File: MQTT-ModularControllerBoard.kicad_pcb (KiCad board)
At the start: 4 copper layers, 200 x 45 mm, 86 parts, among them IC301 LM74700QDBVTQ1, IC401 TPS563200DDCR, IC402 LM74700QDBVTQ1, J301 1715721, J501 A2541HWV-10P, J502 A2541HWV-10P, J503 A2541HWV-10P, J504 A2541HWV-10P, J505 A2541HWV-10P, J506 A2541HWV-10P, J507 A2541HWV-10P, J508 A2541HWV-10P, J601 1051640001, Q301 60V 38A, Q401 60V 38A, U201 ESP32-S3-WROOM-1U-N16R8, U401 LDO 3.3V 1A, U601 ESD Protection IC

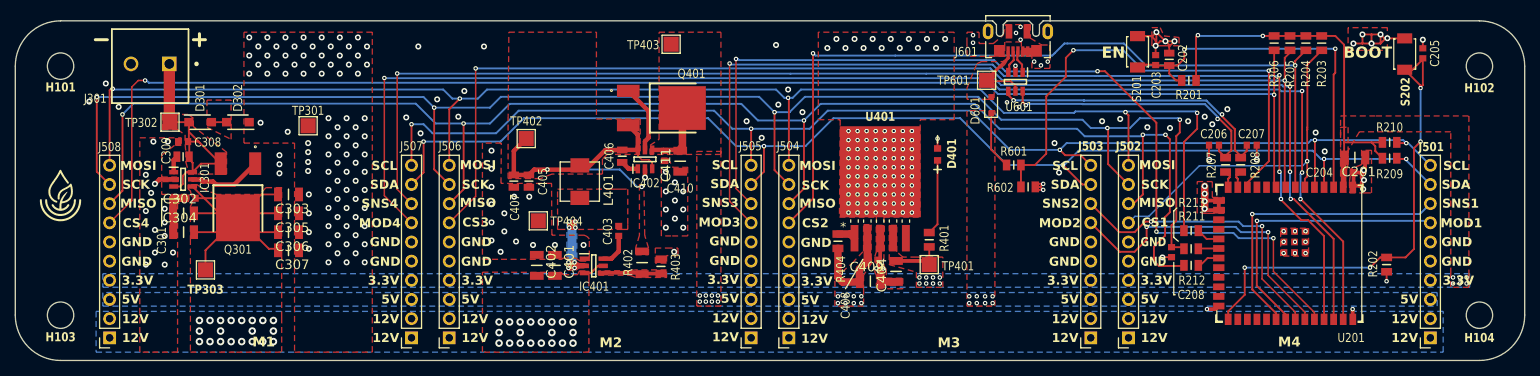
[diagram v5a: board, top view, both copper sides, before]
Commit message: Swapped MCP1826 with a TLV767, and updated the layout and silkscreen to match it.
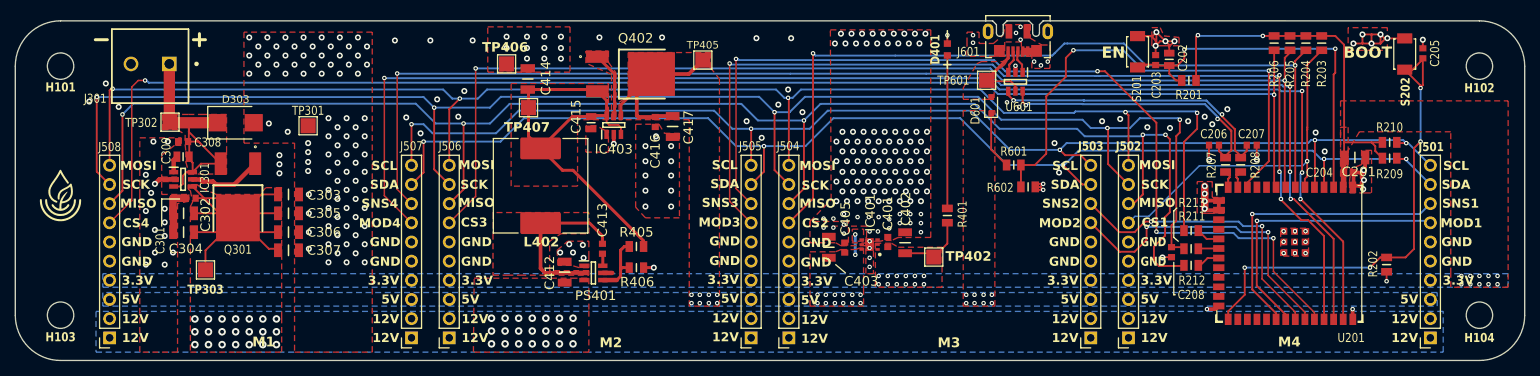
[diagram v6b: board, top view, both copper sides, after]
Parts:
- removed C404, C409, C411: 10uF 10% 25V, JLCPCB Basic:CAPC3216X180N
- removed C406: 220nF 10% 50V, JLCPCB Basic:CAPC2012X135N
- removed C407: 22uF 20% 25V, JLCPCB Basic:CAPC2012X75N
- removed C408, C410: 0.1uF 10% 50V, JLCPCB Basic:CAPC1608X90N
- removed D301, D302: 13.3V 0.1uA Leak, LITTELFUSE Diodes:SODFL3619X98N
- removed IC402: LM74700QDBVTQ1, TEXAS INSTRUMENTS ICs:SOT95P280X145-6N
- removed L401: 3.3uH 6.3A 20%, KOHERELEC Inductors:SMD57x52mm
- removed Q401: 60V 38A, ONSEMI Transistors:DPAK__SINGLE-GAUGE__TO-252_369C__ISSUE_F
- removed R402: 56kΩ 1/4W 1%, YAGEO Resistors:RESC3116X65N
- removed R403, R404: 10kΩ 1/8W 1%, JLCPCB Basic:RESC2013X65N
- removed TP401, TP403, TP404: TestPoint, TestPoint:TestPoint_Pad_2.0x2.0mm
- removed U401: LDO 3.3V 1A, MICROCHIPTECH Low Dropout Regulators:DDPAK5_MC_MCH
- added C412: 10uF 10% 25V, JLCPCB Basic:CAPC3216X180N, F.Cu at (120.3, 124.8)
- added C413: 0.1uF 10% 50V, JLCPCB Basic:CAPC1608X90N, F.Cu at (125.3, 121.7)
- added C414: 47uF 20% 10V, JLCPCB Basic:CAPC3216X190N, F.Cu at (115.4, 99.2)
- added C415: 220nF 10% 50V, JLCPCB Basic:CAPC2012X135N, F.Cu at (123.8, 105.0)
- added C416: 0.1uF 10% 50V, JLCPCB Basic:CAPC1608X90N, F.Cu at (132.3, 104.9)
- added C417: 10uF 10% 25V, JLCPCB Basic:CAPC3216X180N, F.Cu at (134.6, 105.5)
- added D303: 13V 21.5V 1uA Leak, LITTELFUSE Diodes:DO-214AA_Bidirectional, F.Cu at (76.7, 105.0)
- added IC403: LM74700QDBVTQ1, TEXAS INSTRUMENTS ICs:SOT95P280X145-6N, F.Cu at (126.8, 105.3)
- added L402: 10uH, 5.4A, 20%, Inductor_SMD:L_SXN_SMDRI127, F.Cu at (117.1, 113.3)
- added PS401: TPS54308DDCR, TEXAS INSTRUMENTS ICs:SOT95P280X110-6N, F.Cu at (124.1, 124.9)
- added Q402: 60V 38A, ONSEMI Transistors:DPAK__SINGLE-GAUGE__TO-252_369C__ISSUE_F, F.Cu at (133.6, 98.5)
- added R405: 100kΩ 1/8W 1%, JLCPCB Basic:RESC2013X65N, F.Cu at (129.8, 121.4)
- added R406: 13.7kΩ 1/8W 1%, YAGEO Resistors:RESC2012X60N, F.Cu at (129.8, 124.2)
- added TP405: TestPoint, TestPoint:TestPoint_Pad_2.0x2.0mm, F.Cu at (138.6, 96.7)
- added TP406: TestPoint, TestPoint:TestPoint_Pad_2.0x2.0mm, F.Cu at (112.6, 97.2)
- added TP407: TestPoint, TestPoint:TestPoint_Pad_2.0x2.0mm, F.Cu at (115.5, 103.0)
- C401: value 10uF 10% 25V -> 0.1uF 10% 50V; footprint JLCPCB Basic:CAPC3216X180N -> JLCPCB Basic:CAPC1608X90N
- C405: value 22uF 20% 25V -> 10uF 10% 25V; footprint JLCPCB Basic:CAPC2012X75N -> JLCPCB Basic:CAPC3216X180N
- IC401: value TPS563200DDCR -> TLV76733DRVR; footprint TEXAS INSTRUMENTS ICs:SOT95P280X110-6N -> TEXAS INSTRUMENTS ICs:SON65P200X200X80-7N
- moved TP402 56.2 mm to (169.2, 122.8), turned to 0 degrees
- moved C402 48.9 mm to (165.4, 120.9)
- moved C401 44.2 mm to (163.1, 120.8), turned to 90 degrees
- moved C405 40.7 mm to (155.3, 121.5), turned to -90 degrees
- moved IC401 36.7 mm to (160.7, 121.1), turned to 180 degrees
- moved C403 30.0 mm to (157.4, 121.5)
- moved D401 14.0 mm to (171.0, 95.3)
- moved R401 4.00 mm to (171.0, 117.3)
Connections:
- C401 pad 1: GND -> +3V3
- C401 pad 2: +12V -> GND
- C402 pad 2: +12V -> +3V3
- C403 pad 1: Net-(IC401-VBST) -> +5V
- C403 pad 2: Net-(IC401-SW) -> GND
- C405 pad 2: Net-(IC402-ANODE) -> +5V
- IC401 pad 1: GND -> +3V3
- IC401 pad 2: Net-(IC401-SW) -> +3V3
- IC401 pad 3: +12V -> GND
- IC401 pad 4: Net-(IC401-VFB) -> +5V
- IC401 pad 5: +12V -> GND
- IC401 pad 6: Net-(IC401-VBST) -> +5V
- TP402 pad 1: Net-(IC402-ANODE) -> +3V3
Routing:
- net Net-(IC403-ANODE): track 0.00 -> 55.8 mm
- net Net-(IC402-ANODE): track 44.4 -> 0.00 mm, vias 2 -> 0
- net Net-(PS401-SW): track 0.00 -> 21.9 mm
- net Net-(IC401-SW): track 20.7 -> 0.00 mm, vias 8 -> 0
- net GND: track 87.2 -> 76.7 mm, vias 301 -> 326
- net Net-(D401-A): track 10.0 -> 20.3 mm
- net Net-(IC402-GATE): track 9.14 -> 0.00 mm
- net Net-(IC403-GATE): track 0.00 -> 8.77 mm
- net Net-(PS401-FB): track 0.00 -> 8.60 mm
- net Net-(IC401-VFB): track 7.76 -> 0.00 mm
- net Net-(D303-A1): track 34.1 -> 40.5 mm
- net +5V: track 30.4 -> 36.3 mm, vias 24 -> 30
- net Net-(IC401-VBST): track 4.50 -> 0.00 mm
- net +12V: track 63.4 -> 60.5 mm, vias 40 -> 42
- net +3V3: track 60.4 -> 62.8 mm, vias 17 -> 25
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- added copper zone on F.Cu, net Net-(IC403-ANODE)
- added copper zone on F.Cu, net Net-(IC403-GATE)
- added copper zone on F.Cu, net Net-(IC403-VCAP)
- added copper zone on F.Cu, net Net-(PS401-SW)
- removed copper zone on F.Cu, net Net-(D301-A2)
- removed copper zone on B.Cu, net Net-(IC401-SW)
- removed copper zone on F.Cu, net Net-(IC401-SW)
- removed copper zone on F.Cu, net Net-(IC401-VFB)
- removed copper zone on F.Cu, net Net-(IC402-ANODE)

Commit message: Updated layout on pcb slightly.
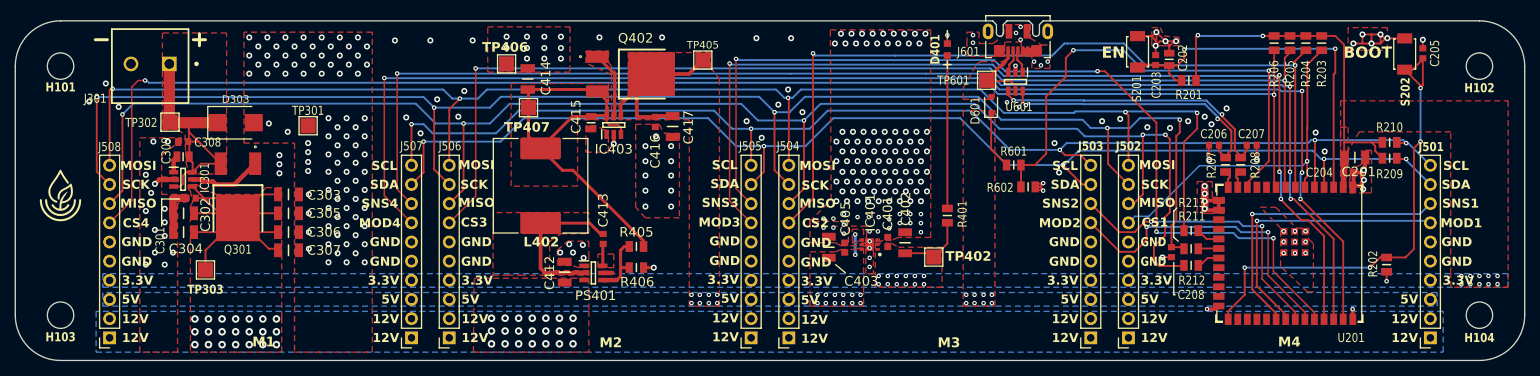
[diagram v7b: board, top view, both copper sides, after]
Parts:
- moved C413 1.30 mm to (125.4, 120.4)
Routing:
- net Net-(PS401-BOOT): track 1.61 -> 2.91 mm
- net Net-(PS401-SW): track 21.9 -> 20.9 mm
- net GND: track 76.7 -> 77.4 mm
- added copper zone on F.Cu, net Net-(PS401-BOOT)
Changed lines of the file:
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@@
 	(footprint "JLCPCB Basic:CAPC1608X90N"
 		(layer "F.Cu")
-		(at 125.3 121.7 -90)
+		(at 125.4 120.4 -90)
 		(descr "0603")
 		(tags "Capacitor")
@@
 	)
 	(segment
+		(start 183.3 113.5)
+		(end 183.7 113.9)
+		(width 0.25)
+		(layer "F.Cu")
+		(net 2)
+	)
+	(segment
 		(start 181.65 95.564201)
 		(end 182.723599 95.564201)
@@
 	)
 	(segment
-		(start 211.99 109.69)
-		(end 211.99 107.975)
+		(start 183.7 113.9)
+		(end 183.7 114)
 		(width 0.25)
 		(layer "F.Cu")
@@
 	)
 	(segment
-		(start 183.05 113.1)
-		(end 182.65 113.5)
+		(start 211.99 109.69)
+		(end 211.99 107.975)
 		(width 0.25)
 		(layer "F.Cu")
@@
 	)
 	(segment
-		(start 201.1 94.2)
-		(end 199.9 94.2)
-		(width 0.25)
-		(layer "F.Cu")
-		(net 2)
-	)
-	(segment
 		(start 199.9 94.2)
 		(end 200.4 94.7)
@@
 	)
 	(segment
-		(start 200.4 94.9)
-		(end 201.1 94.2)
-		(width 0.25)
-		(layer "F.Cu")
-		(net 2)
-	)
-	(segment
 		(start 226.2 112.6)
 		(end 225.9 112.9)
@@
 	)
 	(segment
+		(start 183.7 113)
+		(end 183.6 113.1)
+		(width 0.25)
+		(layer "F.Cu")
+		(net 2)
+	)
+	(segment
 		(start 228.4 94.5)
 		(end 227.2 94.5)
@@
 	)
 	(segment
+		(start 183.6 113.1)
+		(end 183.05 113.1)
+		(width 0.25)
+		(layer "F.Cu")
+		(net 2)
+	)
+	(segment
 		(start 126.8 106.65)
 		(end 126.8 107.8)
@@
 	)
 	(segment
-		(start 183.3 113.5)
-		(end 183.7 113.9)
-		(width 0.25)
-		(layer "F.Cu")
-		(net 2)
-	)
-	(segment
 		(start 171 93.4)
 		(end 171 94.5125)
@@
 	)
 	(segment
+		(start 183.05 113.1)
+		(end 182.65 113.5)
+		(width 0.25)
+		(layer "F.Cu")
+		(net 2)
+	)
+	(segment
 		(start 205.66 107.985)
 		(end 205.67 107.975)
@@
 	)
 	(segment
+		(start 201.3 94.2)
+		(end 199.9 94.2)
+		(width 0.25)
+		(layer "F.Cu")
+		(net 2)
+	)
+	(segment
 		(start 199.2 94.2)
 		(end 198.6 94.8)
@@
 	)
 	(segment
+		(start 200.4 94.9)
+		(end 201.1 94.2)
+		(width 0.25)
+		(layer "F.Cu")
+		(net 2)
+	)
+	(segment
 		(start 198.7 93)
 		(end 198.175 93.525)
@@
 	)
 	(segment
+		(start 183.6 113.9)
+		(end 183.05 113.9)
+		(width 0.25)
+		(layer "F.Cu")
+		(net 2)
+	)
+	(segment
 		(start 198.7 93)
 		(end 198.7 94.7)
@@
 	)
 	(segment
-		(start 183.3 113.5)
-		(end 183.7 113.1)
-		(width 0.25)
-		(layer "F.Cu")
-		(net 2)
-	)
-	(segment
 		(start 226.35 111.135)
 		(end 226.35 109.6)
@@
 	)
 	(segment
-		(start 183.7 113.9)
-		(end 183.05 113.9)
-		(width 0.25)
-		(layer "F.Cu")
-		(net 2)
-	)
-	(segment
-		(start 183.7 113.1)
-		(end 183.05 113.1)
+		(start 205.7 109.9)
+		(end 205.7 109.7)
 		(width 0.25)
 		(layer "F.Cu")
@@
 	)
 	(segment
-		(start 205.7 109.9)
-		(end 205.7 109.7)
+		(start 200.7 122.81)
+		(end 199.54 122.81)
 		(width 0.25)
 		(layer "F.Cu")
@@
 	)
 	(segment
-		(start 200.7 122.81)
-		(end 199.54 122.81)
+		(start 183.7 114)
+		(end 183.6 113.9)
 		(width 0.25)
 		(layer "F.Cu")
@@
 	)
 	(segment
-		(start 183.05 113.9)
-		(end 182.65 113.5)
-		(width 0.25)
-		(layer "F.Cu")
-		(net 2)
-	)
-	(segment
 		(start 180.023658 97.453659)
 		(end 180.023658 98.323658)
@@
 	)
 	(segment
+		(start 183.7 113.1)
+		(end 183.7 113)
+		(width 0.25)
+		(layer "F.Cu")
+		(net 2)
+	)
+	(segment
 		(start 224.7 131.03)
 		(end 224.72 131.05)
@@
 	)
 	(segment
+		(start 183.3 113.5)
+		(end 183.7 113.1)
+		(width 0.25)
+		(layer "F.Cu")
+		(net 2)
+	)
+	(segment
 		(start 226.07 111.6)
 		(end 224.82 111.6)
@@
 	)
 	(segment
+		(start 201.1 94.2)
+		(end 201.3 94.2)
+		(width 0.25)
+		(layer "F.Cu")
+		(net 2)
+	)
+	(segment
 		(start 66.6 112.5)
 		(end 66 113.1)
@@
 		(net 2)
 	)
+	(segment
+		(start 183.05 113.9)
+		(end 182.65 113.5)
+		(width 0.25)
+		(layer "F.Cu")
+		(net 2)
+	)
 	(via
 		(at 165.9 94.5)
@@
 	)
 	(via
-		(at 206.1 105.2)
+		(at 206 105.2)
 		(size 0.8)
 		(drill 0.4)
@@
 	)
 	(via
-		(at 208.1 103.2)
+		(at 208 103.1)
 		(size 0.8)
 		(drill 0.4)
@@
 	)
 	(via
-		(at 201.1 94.2)
+		(at 201.3 94.2)
 		(size 0.8)
 		(drill 0.4)
@@
 	)
 	(via
-		(at 183.7 113.9)
+		(at 183.7 114)
 		(size 0.6)
 		(drill 0.3)
@@
 	)
 	(via
-		(at 183.7 113.1)
+		(at 183.7 113)
 		(size 0.6)
 		(drill 0.3)
@@
 	)
 	(segment
-		(start 125.35 123.95)
-		(end 125.35 122.41)
+		(start 125.35 121.11)
+		(end 125.4 121.06)
 		(width 0.4)
 		(layer "F.Cu")
@@
 	)
 	(segment
-		(start 125.35 122.41)
-		(end 125.3 122.36)
+		(start 125.35 123.95)
+		(end 125.35 121.11)
 		(width 0.4)
 		(layer "F.Cu")
@@
 	)
 	(segment
-		(start 117.1 124.3)
-		(end 117.1 118.3)
-		(width 0.5)
+		(start 125.04 119.74)
+		(end 123.6 118.3)
+		(width 0.4)
 		(layer "F.Cu")
 		(net 12)
 	)
 	(segment
-		(start 123.6 118.3)
+		(start 117.1 124.3)
 		(end 117.1 118.3)
-		(width 0.4)
+		(width 0.5)
 		(layer "F.Cu")
 		(net 12)
 	)
 	(segment
-		(start 125.3 121.04)
-		(end 125.3 120)
-		(width 0.4)
+		(start 122.85 124.9)
+		(end 117.7 124.9)
+		(width 0.5)
 		(layer "F.Cu")
 		(net 12)
 	)
 	(segment
-		(start 122.85 124.9)
-		(end 117.7 124.9)
-		(width 0.5)
+		(start 125.4 119.74)
+		(end 125.04 119.74)
+		(width 0.4)
 		(layer "F.Cu")
 		(net 12)
 	)
 	(segment
-		(start 125.3 120)
-		(end 123.6 118.3)
+		(start 123.6 118.3)
+		(end 117.1 118.3)
 		(width 0.4)
 		(layer "F.Cu")
@@
 		(polygon
 			(pts
-				(xy 70.4 111.8) (xy 75.5 111.8) (xy 75.5 108.9) (xy 75.5 103.9) (xy 72.5 103.9) (xy 70.4 103.9)
-				(xy 67 103.9) (xy 67 105.9) (xy 69 105.9) (xy 70 106.6) (xy 70 107.9) (xy 70.1 108.8) (xy 70.1 110.2)
-				(xy 70.4 111.3)
+				(xy 70.4 111.8) (xy 75.5 111.8) (xy 75.5 108.9) (xy 75.5 93.1) (xy 67 93.1) (xy 67 105.9) (xy 69 105.9)
+				(xy 70 106.6) (xy 70 107.9) (xy 70.1 108.8) (xy 70.1 110.2) (xy 70.4 111.3)
 			)
 		)
@@
 	)
 	(zone
+		(net 11)
+		(net_name "Net-(PS401-BOOT)")
+		(layer "F.Cu")
+		(hatch edge 0.5)
+		(priority 21)
+		(connect_pads yes
+			(clearance 0)
+		)
+		(min_thickness 0.25)
+		(filled_areas_thickness no)
+		(fill yes
+			(thermal_gap 0.5)
+			(thermal_bridge_width 0.5)
+		)
+		(polygon
+			(pts
+				(xy 124.7 124.2) (xy 124.7 122.4) (xy 126.8 122.4) (xy 126.8 124.2)
+			)
+		)
+	)
+	(zone
 		(net 2)
 		(net_name "GND")
@@
 		(polygon
 			(pts
-				(xy 218.86 118.975) (xy 218.86 122.675) (xy 215.16 122.675) (xy 215.16 118.975)
+				(xy 212.5 116.2) (xy 214.5 116.2) (xy 217.3 118.975) (xy 218.86 118.975) (xy 218.86 120.4) (xy 219.5 121)
+				(xy 219.5 127.4) (xy 218.7 127.4) (xy 215.154973 124.029235) (xy 215.16 122.675) (xy 215.16 118.975)
 			)
 		)

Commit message: Updated and tweaked PCB layout.
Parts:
- moved R405 2.42 mm to (127.7, 120.2), turned to 90 degrees
- moved D601 1.60 mm to (175.2, 102.7)
- moved C401 1.20 mm to (164.3, 120.8)
- moved IC401 1.20 mm to (161.9, 121.1)
- moved TP402 1.20 mm to (170.4, 122.8)
- moved C402 1.20 mm to (166.6, 120.9)
- moved C403 1.20 mm to (158.6, 121.5)
- moved C405 1.20 mm to (156.5, 121.5)
- moved D401 0.64 mm to (171.5, 94.9)
- moved R401 0.50 mm to (171.5, 117.3)
- moved R406 0.40 mm to (129.8, 123.8)
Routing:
- net Net-(IC403-ANODE): track 55.8 -> 52.4 mm
- net +5V: track 36.3 -> 37.0 mm
- net Net-(PS401-FB): track 8.60 -> 7.99 mm
